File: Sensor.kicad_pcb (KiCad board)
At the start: 2 copper layers, 49 x 49 mm, 52 parts, among them IC1 STM32L051K8T6, P1 CONN_02X04, P2 CONN_02X04, P3 CONN_01X02, Q1 AO3401, SW1 SW_PUSH, SW2 SW_PUSH, U1 MCP60x4, U2 HTU21D, U3 PIR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

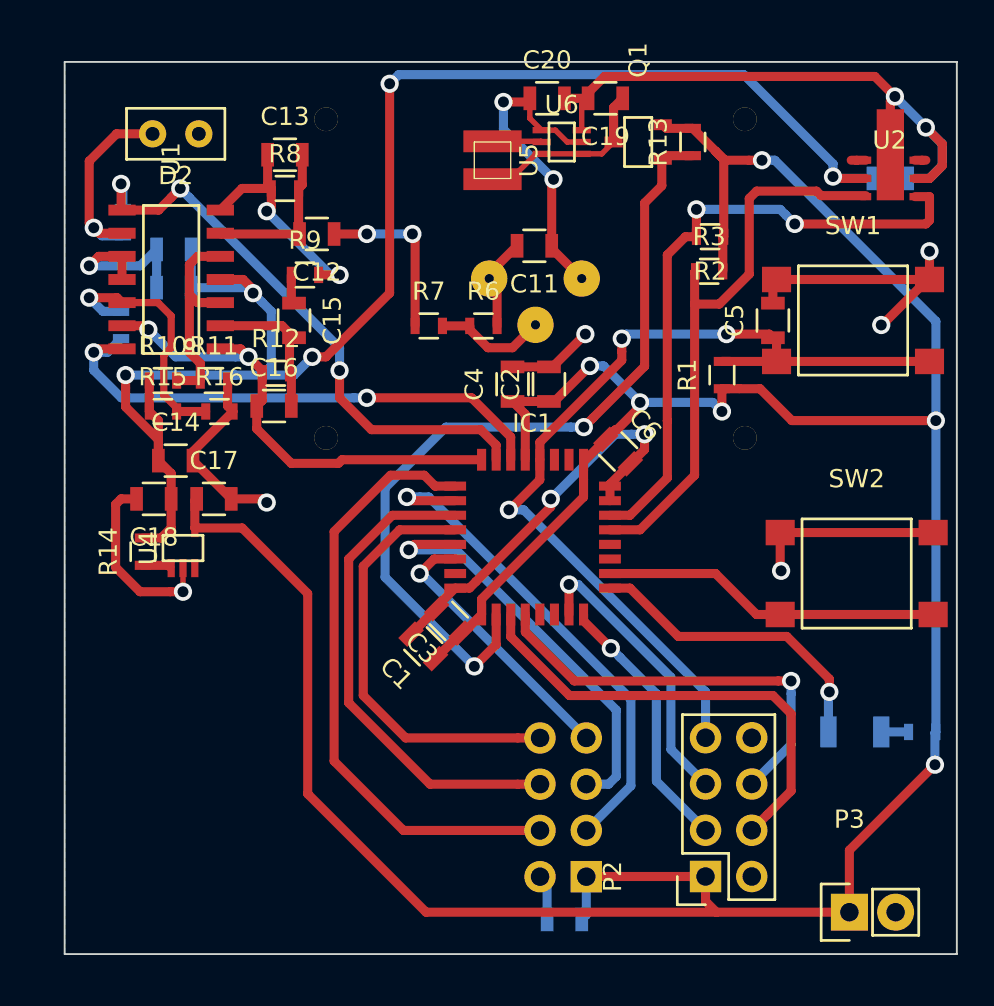
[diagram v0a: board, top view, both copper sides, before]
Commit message: Corrections I2C and Dig Opamp out
 * Fix level shift for I2C
 * Fix level shift opamp digital out (PIR)

Signed-off-by: Philip Luyckx <philip.luyckx@gmail.com>
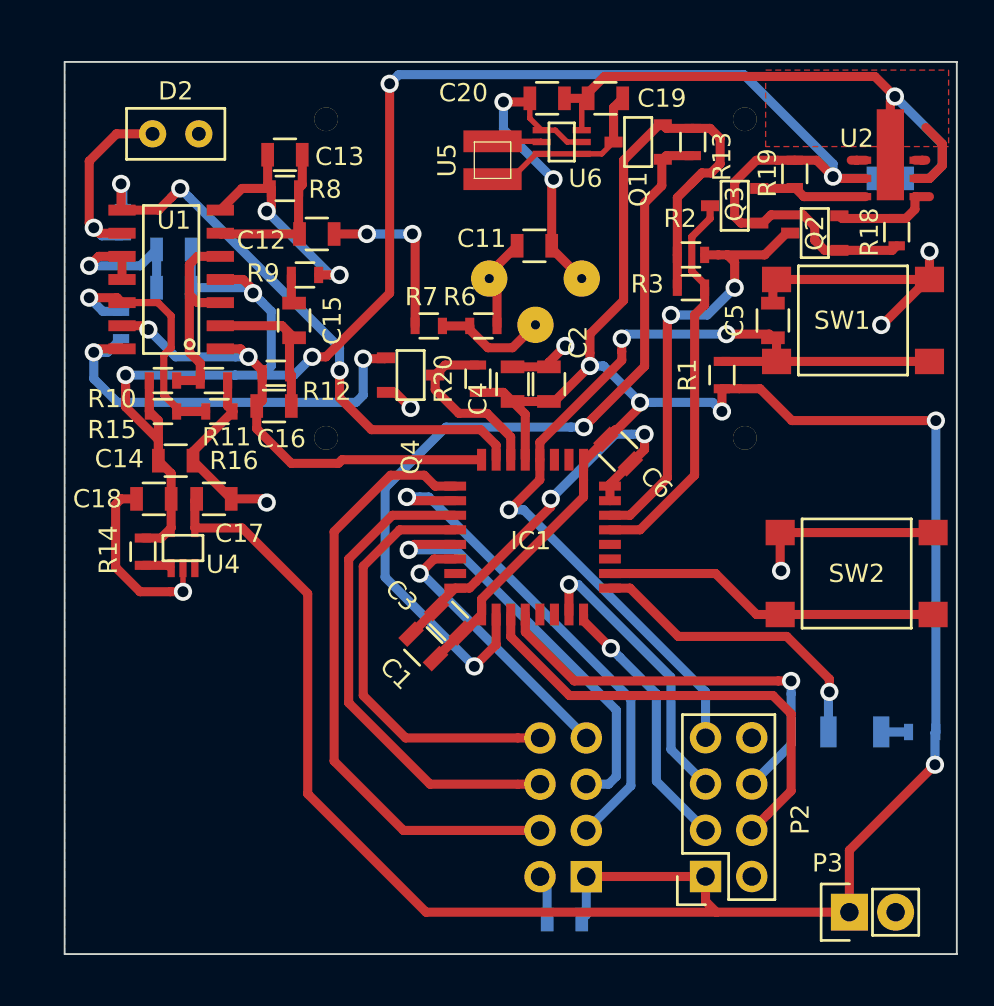
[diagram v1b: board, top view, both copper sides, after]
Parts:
- added Q2: NMosfetGen, CustomSmd:SOT23, F.Cu at (159.6, 78.7)
- added Q3: NMosfetGen, CustomSmd:SOT23, F.Cu at (155.2, 77.2)
- added Q4: Q_NMOS_GSD, CustomSmd:SOT23, F.Cu at (137.4, 86.5)
- added R18: 10k, Resistors_SMD:R_0603, F.Cu at (164.1, 78.7)
- added R19: 10k, Resistors_SMD:R_0603, F.Cu at (158.5, 75.5)
- added R20: 100k, Resistors_SMD:R_0603, F.Cu at (141.1, 86.7)
- moved R2 1.45 mm to (152.8, 79.9), turned to 0 degrees
- moved R3 1.35 mm to (152.8, 81.7), turned to 180 degrees
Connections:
- IC1 pad 29: HTU21_SCK -> Net-(IC1-Pad29)
- IC1 pad 30: HTU21_SDA -> Net-(IC1-Pad30)
- R17 pad 1: DIG_Motion -> Net-(Q4-Pad1)
- R2 pad 2: HTU21_SDA -> Net-(IC1-Pad30)
- R3 pad 1: HTU21_SCK -> Net-(IC1-Pad29)
- U1 pad 14: DIG_Motion -> Net-(Q4-Pad1)
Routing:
- net HTU21_SDA: track 35.1 -> 5.92 mm, vias 2 -> 0
- net HTU21_SCK: track 31.6 -> 6.08 mm
- net Net-(IC1-Pad30): track 0.00 -> 24.3 mm, vias 0 -> 2
- net Net-(Q4-Pad1): track 0.00 -> 23.7 mm, vias 0 -> 2
- net Net-(IC1-Pad29): track 0.00 -> 21.6 mm
- net DIG_Motion: track 30.1 -> 9.85 mm, vias 2 -> 0
- net +1V8: track 88.0 -> 106.8 mm
- net +BATT: track 174.1 -> 173.3 mm, vias 6 -> 5
- net GND: track 126.6 -> 127.2 mm
- added copper zone on F.Cu, net GND

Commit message: Update connectors to custom ones
Signed-off-by: Philip Luyckx <philip.luyckx@gmail.com>
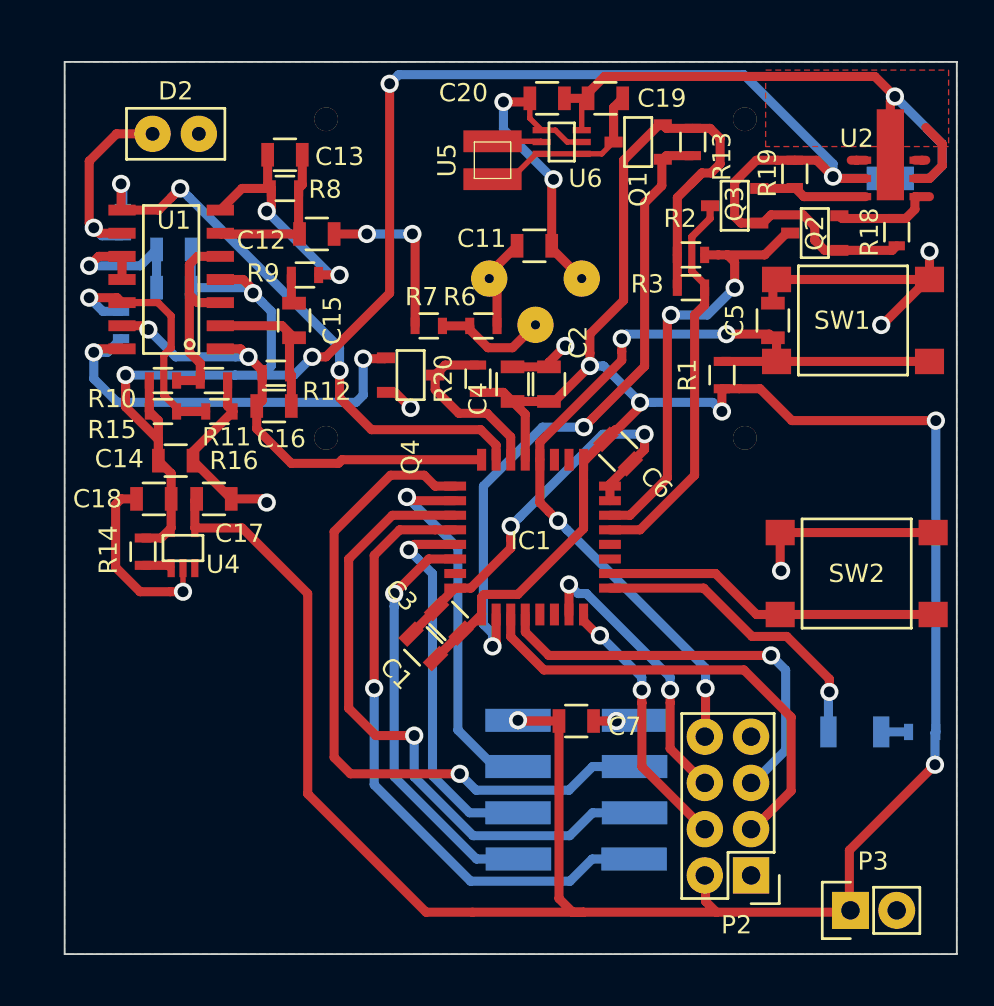
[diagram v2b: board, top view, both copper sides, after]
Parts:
- C7: moved to F.Cu
- P1: footprint Socket_Strips:Socket_Strip_Straight_2x04 -> PinHeaders:Pin_Header_Straight_2x04_SMD
- P2: footprint Socket_Strips:Socket_Strip_Straight_2x04 -> PinHeaders:Pin_Header_Straight_2x04_TH
- P3: footprint Socket_Strips:Socket_Strip_Straight_1x02 -> PinHeaders:Pin_Header_Straight_1x02_TH
- moved C7 10.9 mm to (146.5, 105.5), turned to 180 degrees
- moved P1 6.07 mm to (146.5, 108.0), turned to 270 degrees
- moved P2 2.50 mm to (156.1, 114.0), turned to 180 degrees
- moved P3 0.12 mm to (161.6, 115.9), turned to 90 degrees
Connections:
- P1 pad 1: +BATT -> GND
- P1 pad 2: GND -> +BATT
- P1 pad 3: RF_CSN -> RF_CE
- P1 pad 4: RF_CE -> RF_CSN
- P1 pad 5: SPI_RF_MOSI -> SPI_RF_SCK
- P1 pad 6: SPI_RF_SCK -> SPI_RF_MOSI
- P1 pad 7: RF_IRQ -> SPI_RF_MISO
- P1 pad 8: SPI_RF_MISO -> RF_IRQ
- P2 pad 1: +BATT -> GND
- P2 pad 2: GND -> +BATT
- P2 pad 3: SWDCLK -> UART_TX
- P2 pad 4: UART_TX -> SWDCLK
- P2 pad 5: SWDIO -> UART_RX
- P2 pad 6: UART_RX -> SWDIO
- P2 pad 7: MCU_RST -> Net-(P2-Pad7)
- P2 pad 8: Net-(P2-Pad8) -> MCU_RST
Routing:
- net SPI_RF_MISO: track 23.7 -> 35.8 mm, vias 0 -> 1
- net Enable5V: track 45.7 -> 35.9 mm
- net SPI_RF_SCK: track 27.1 -> 35.6 mm, vias 0 -> 1
- net RF_IRQ: track 15.2 -> 23.2 mm
- net RF_CSN: track 27.9 -> 20.8 mm
- net +BATT: track 173.3 -> 180.2 mm, vias 5 -> 6
- net RF_CE: track 33.7 -> 39.0 mm, vias 0 -> 1
- net SPI_RF_MOSI: track 23.2 -> 21.2 mm
- net MCU_RST: track 50.7 -> 48.8 mm, vias 3 -> 4
- net GND: track 127.2 -> 127.5 mm, vias 11 -> 12
- net SWDCLK: track 14.6 -> 14.7 mm, vias 1 -> 2
- net SWDIO: vias 1 -> 2

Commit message: Add prices
Signed-off-by: Philip Luyckx <philip.luyckx@gmail.com>
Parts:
- R1: value 100k -> 10k
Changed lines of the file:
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@@
     (links 141)
     (no_connects 0)
-    (area 118.349999 56.2 188.347166 120.987333)
+    (area 118.349999 69.249999 167.450001 118.350001)
     (thickness 1.6)
     (drawings 10)
@@
       (effects (font (size 1 1) (thickness 0.15)))
     )
-    (fp_text value 100k (at 0 1.9 90) (layer F.Fab)
-      (effects (font (size 1 1) (thickness 0.15)))
-    )
+    (fp_text value 10k (at 0 1.9 90) (layer F.Fab)
+      (effects (font (size 1 1) (thickness 0.15)))
+    )

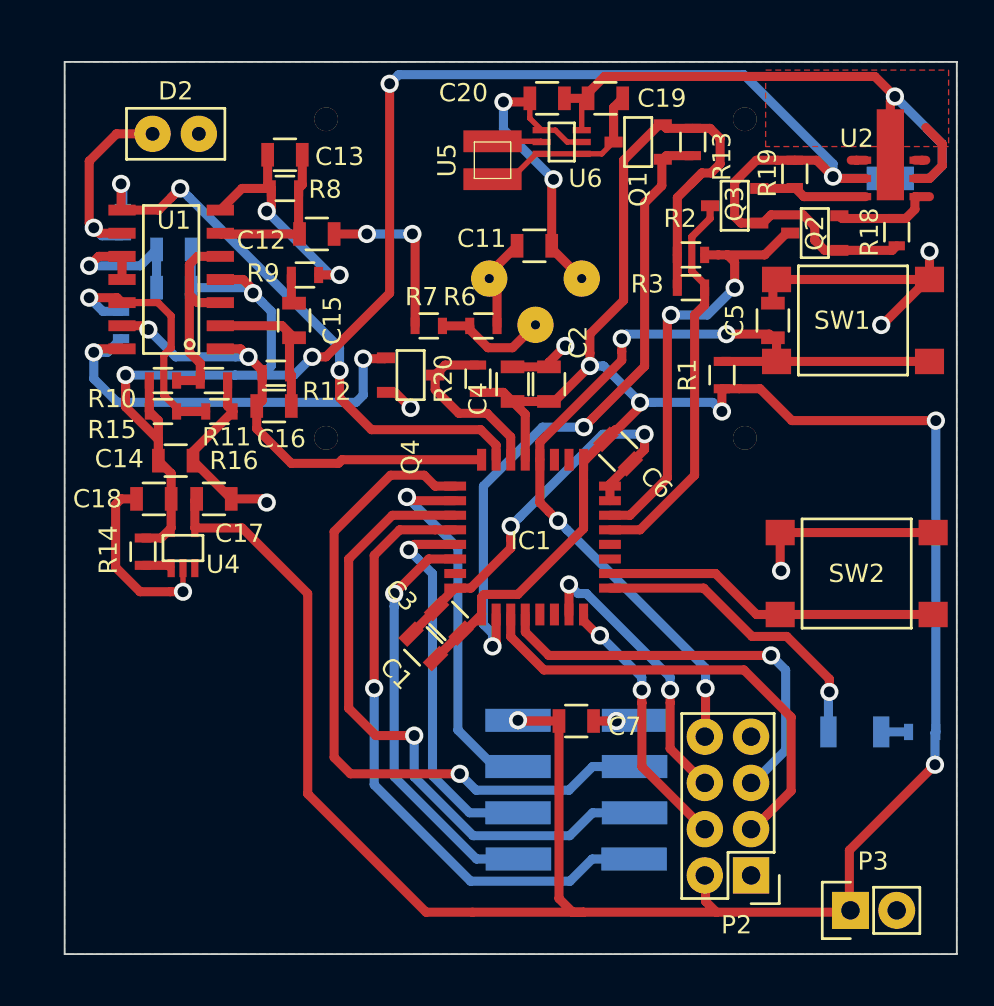
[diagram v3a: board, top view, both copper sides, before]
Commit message: Update connector for Vin
Signed-off-by: Philip Luyckx <philip.luyckx@gmail.com>
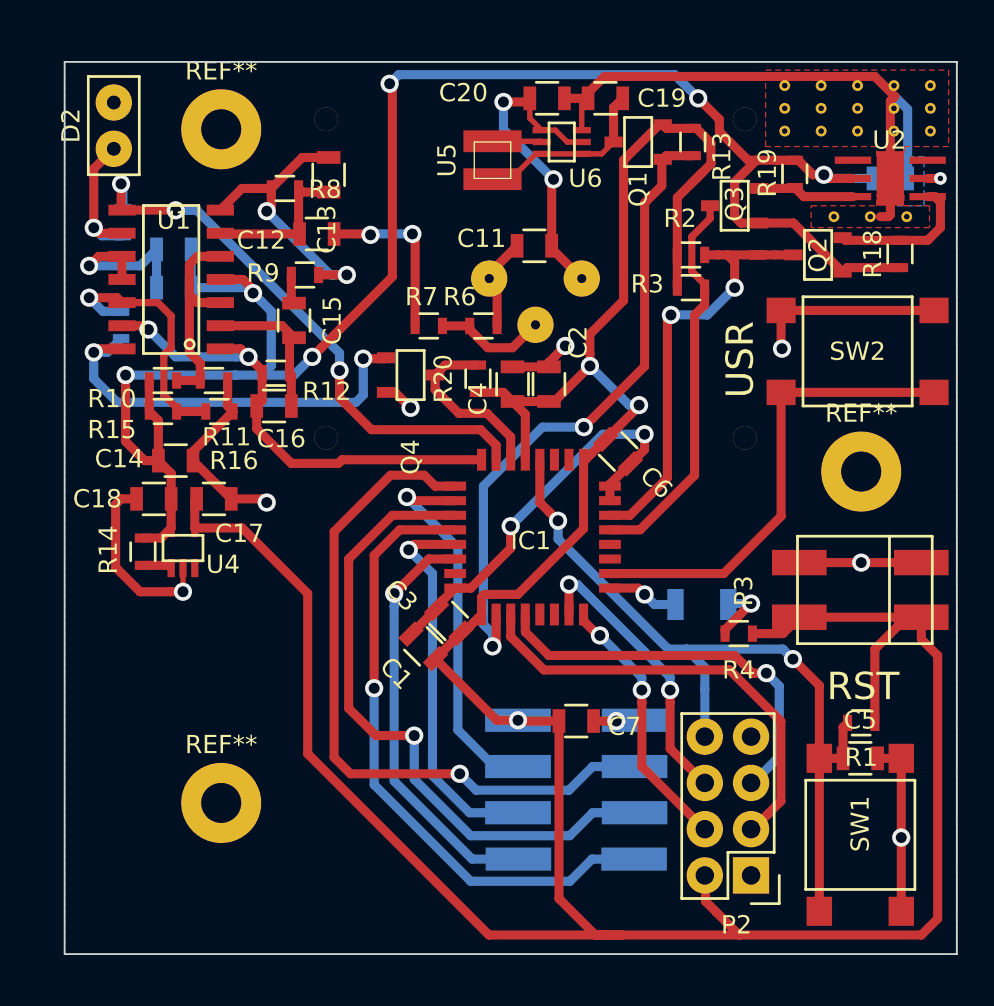
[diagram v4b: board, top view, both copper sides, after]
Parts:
- added REF**: 1pin, Connect:1pin, F.Cu at (163.9, 73.1)
- added REF**: 1pin, Connect:1pin, F.Cu at (159.9, 70.6)
- added REF**: 1pin, Connect:1pin, F.Cu at (165.9, 71.8)
- added REF**: 1pin, Connect:1pin, F.Cu at (163.9, 71.8)
- added REF**: 1pin, Connect:1pin, F.Cu at (157.9, 71.8)
- added REF**: 1pin, Connect:1pin, F.Cu at (159.9, 71.8)
- added REF**: 1pin, Connect:1pin, F.Cu at (161.9, 71.8)
- added REF**: 1pin, Connect:1pin, F.Cu at (164.7, 77.8)
- added REF**: 1pin, Connect:1pin, F.Cu at (162.7, 77.8)
- added REF**: 1pin, Connect:1pin, F.Cu at (160.7, 77.8)
- added REF**: MountingHole_2.2mm_M2_Pad, Mounting_Holes:MountingHole_2.2mm_M2_Pad, F.Cu at (127.0, 73.0)
- added REF**: 1pin, Connect:1pin, F.Cu at (165.9, 73.1)
- added REF**: MountingHole_2.2mm_M2_Pad, Mounting_Holes:MountingHole_2.2mm_M2_Pad, F.Cu at (162.2, 91.8)
- added REF**: MountingHole_2.2mm_M2_Pad, Mounting_Holes:MountingHole_2.2mm_M2_Pad, F.Cu at (127.0, 110.0)
- added REF**: 1pin, Connect:1pin, F.Cu at (157.9, 73.1)
- added REF**: 1pin, Connect:1pin, F.Cu at (161.9, 73.1)
- added REF**: 1pin, Connect:1pin, F.Cu at (159.9, 73.1)
- added REF**: 1pin, Connect:1pin, F.Cu at (163.9, 70.6)
- added REF**: 1pin, Connect:1pin, F.Cu at (165.9, 70.6)
- added REF**: 1pin, Connect:1pin, F.Cu at (157.9, 70.6)
- added REF**: 1pin, Connect:1pin, F.Cu at (161.9, 70.6)
- P3: footprint PinHeaders:Pin_Header_Straight_1x02_TH -> ConnWago:ConnWago_2059_2P_SMD
- R4: moved to F.Cu
- moved SW1 28.3 mm to (162.1, 111.8), turned to 90 degrees
- moved C5 24.5 mm to (162.1, 107.5), turned to 0 degrees
- moved R1 20.6 mm to (162.2, 105.6), turned to 180 degrees
- moved P3 19.4 mm to (165.2, 96.8), turned to 270 degrees
- moved SW2 12.2 mm to (161.9, 85.2)
- moved R4 11.4 mm to (155.4, 100.7)
- moved D1 10.9 mm to (153.4, 99.1)
- moved D2 3.43 mm to (121.1, 72.8), turned to 90 degrees
- moved C13 2.64 mm to (132.9, 75.5), turned to 270 degrees
- moved Q2 1.21 mm to (159.8, 79.9)
- moved R18 1.21 mm to (164.3, 79.8)
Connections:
- P3 pad 1: +BATT -> GND
- P3 pad 2: GND -> +BATT
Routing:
- net MCU_LED: track 17.0 -> 3.97 mm
- net BTN_User: track 18.7 -> 26.3 mm
- net MCU_RST: track 48.8 -> 43.4 mm, vias 4 -> 2
- net +1V8: track 106.8 -> 102.4 mm, vias 5 -> 6
- net Net-(D2-Pad1): track 11.3 -> 8.25 mm
- net Net-(C13-Pad1): track 13.2 -> 15.9 mm
- net HTU21_SDA: track 5.92 -> 7.95 mm
- net Net-(D1-Pad2): track 1.50 -> 3.51 mm, vias 0 -> 1
- net ADC_Light: track 32.9 -> 31.0 mm
- net UART_RX: track 23.2 -> 22.1 mm
- net GND: track 127.5 -> 126.5 mm
- net UART_TX: track 25.6 -> 24.6 mm
- net Net-(U2-Pad4): track 0.80 -> 0.00 mm
- net HTU21_SCK: track 6.08 -> 5.38 mm
- net Net-(U2-Pad3): track 0.60 -> 0.00 mm
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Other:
- board text added: "RST"
- board text added: "USR"

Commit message: Finish layout
Signed-off-by: Philip Luyckx <philip.luyckx@gmail.com>
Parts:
- moved SW2 13.9 mm to (162.4, 99.0), turned to 90 degrees
- moved P3 13.8 mm to (164.7, 83.0)
- moved R4 5.54 mm to (160.2, 97.9)
- moved P2 1.88 mm to (155.4, 112.2)
- moved D1 1.26 mm to (153.0, 97.9)
- moved REF** 0.96 mm to (161.7, 91.0)
- moved SW1 0.83 mm to (162.5, 111.0)
- moved C5 0.78 mm to (162.4, 106.8)
- moved R1 0.67 mm to (162.4, 105.0)
- moved C16 0.22 mm to (129.7, 88.1)
- moved C6 0.22 mm to (148.6, 90.6)
- moved Q1 0.22 mm to (149.7, 73.6)
- moved R13 0.22 mm to (152.7, 73.6)
- moved R2 0.22 mm to (152.6, 79.8)
- moved R3 0.22 mm to (152.6, 81.6)
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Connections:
- P2 pad 1: GND -> +BATT
- P2 pad 2: +BATT -> GND
- P2 pad 3: UART_TX -> SWDCLK
- P2 pad 4: SWDCLK -> UART_TX
- P2 pad 5: UART_RX -> SWDIO
- P2 pad 6: SWDIO -> UART_RX
- P2 pad 7: Net-(P2-Pad7) -> MCU_RST
- P2 pad 8: MCU_RST -> Net-(P2-Pad8)
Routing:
- net +BATT: track 180.3 -> 197.0 mm
- net UART_RX: track 22.1 -> 13.0 mm, vias 1 -> 0
- net UART_TX: track 24.6 -> 15.9 mm
- net GND: track 126.5 -> 119.7 mm, vias 12 -> 13
- net SWDCLK: track 14.7 -> 21.0 mm, vias 2 -> 0
- net BTN_User: track 26.3 -> 21.5 mm, vias 0 -> 2
- net SWDIO: track 16.0 -> 17.7 mm, vias 2 -> 0
- net MCU_RST: track 43.4 -> 45.1 mm, vias 2 -> 3
- net Net-(D1-Pad2): track 3.51 -> 5.00 mm
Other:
- board text added: "GND"
- board text added: "V+"
